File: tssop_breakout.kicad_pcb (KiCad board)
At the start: 2 copper layers, 16 x 49 mm, 3 parts, among them P1 CONN_01X19, P2 CONN_01X19, U1 MSP430G2955IDA38

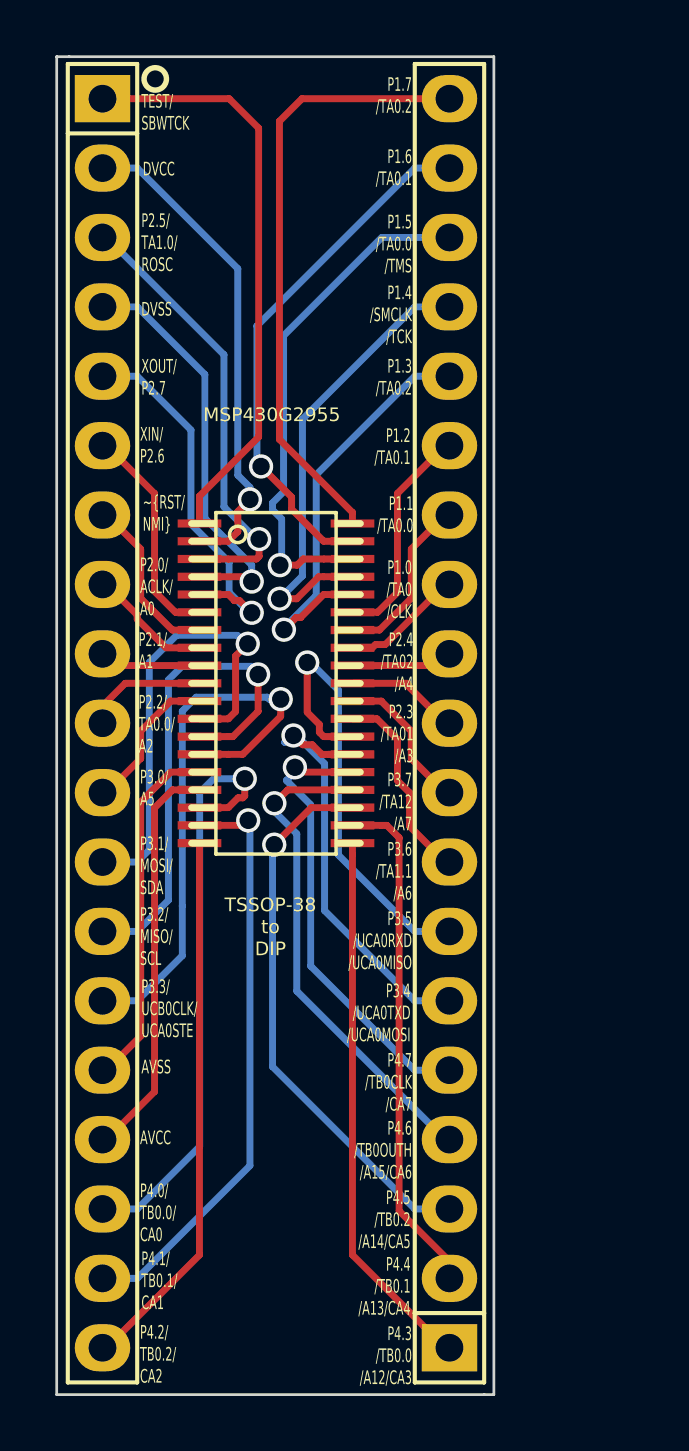
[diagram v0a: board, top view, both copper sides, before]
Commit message: changed wrong footprint
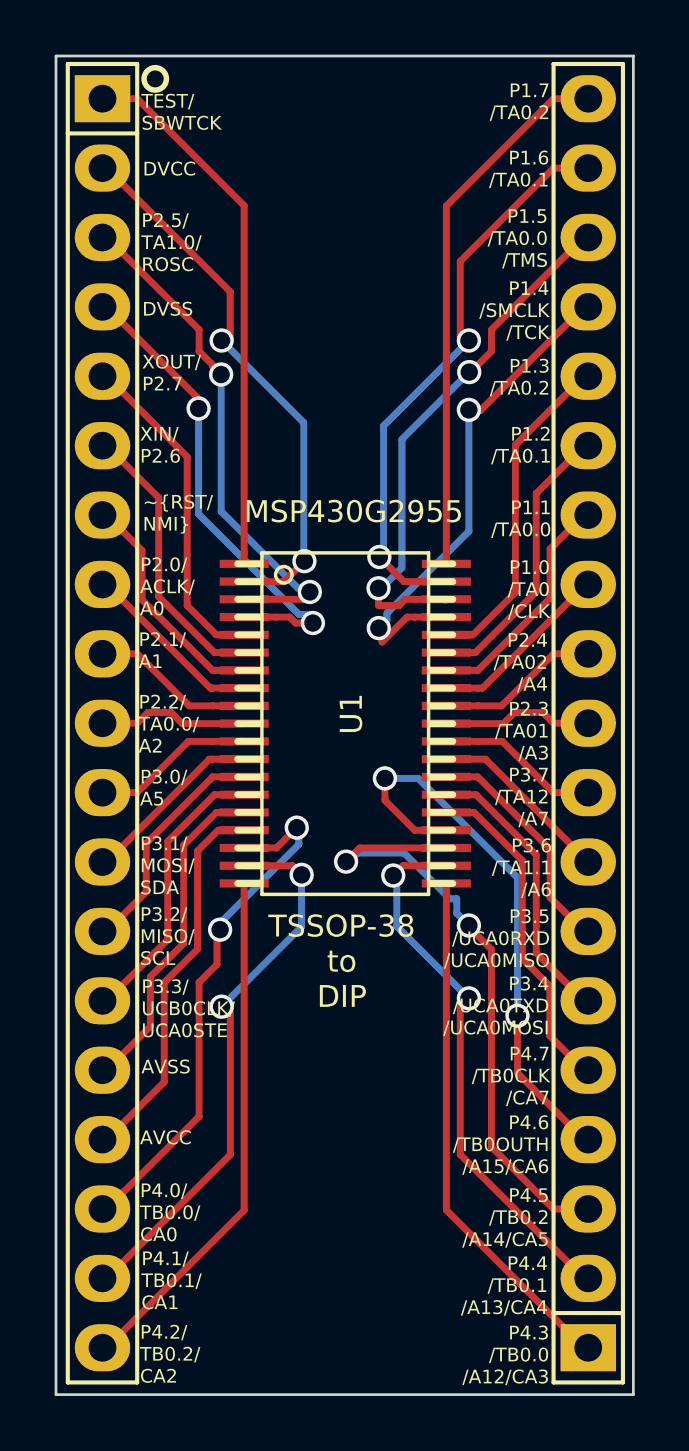
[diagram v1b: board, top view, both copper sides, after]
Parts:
- U1: footprint SMD_Packages:AB2_TSSOP38 -> SMD_Packages:AB2_TSSOP38_W
- moved P2 5.08 mm to (118.4, 119.2)
- moved U1 2.93 mm to (109.5, 119.2)
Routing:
- net /12: track 17.0 -> 6.75 mm, vias 1 -> 0
- net /14: track 20.6 -> 10.4 mm, vias 1 -> 0
- net /13: track 18.5 -> 8.57 mm, vias 1 -> 0
- net /26: track 16.8 -> 8.57 mm, vias 1 -> 0
- net /25: track 16.8 -> 10.4 mm, vias 1 -> 0
- net /24: track 16.6 -> 12.3 mm, vias 1 -> 0
- net /34: track 15.7 -> 12.3 mm, vias 1 -> 0
- net /3: track 16.4 -> 19.5 mm, vias 1 -> 2
- net /4: track 15.0 -> 17.8 mm, vias 1 -> 2
- net /22: track 20.2 -> 22.9 mm, vias 1 -> 2
- net /17: track 21.8 -> 19.3 mm, vias 1 -> 2
- net /2: track 18.0 -> 20.5 mm, vias 1 -> 2
- net /38: track 22.4 -> 19.9 mm
- net /23: track 18.3 -> 20.6 mm, vias 1 -> 2
- net /6: track 8.17 -> 10.4 mm
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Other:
- board size 16 x 49 mm -> 21.1 x 49 mm
